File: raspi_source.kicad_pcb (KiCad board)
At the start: 2 copper layers, 18 parts, among them J1 Conn_01x02_Female, J2 Conn_01x01_Female, J3 Conn_01x01_Female, J4 Conn_01x01_Female, J5 Conn_01x02_Female, Q1 2N7000, Q2 DMG3415U, U1 OKL-T

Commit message: expand footprints
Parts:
- removed C1, C2: CP1, Capacitors_THT:CP_Radial_Tantal_D4.5mm_P2.50mm
- added CP1: 100u, Capacitors_THT:CP_Radial_Tantal_D4.5mm_P2.50mm, F.Cu at (193.0, 94.0)
- added CP2: 47u, Capacitors_THT:CP_Radial_Tantal_D4.5mm_P2.50mm, F.Cu at (160.0, 135.9)
- added CP3: 0.1u, Capacitors_THT:CP_Radial_Tantal_D4.5mm_P2.50mm, F.Cu at (130.8, 120.7)
- added Q3: 2N7000, TO_SOT_Packages_THT:TO-92_Molded_Narrow, F.Cu at (109.2, 138.4)
- added R6: 330, Resistors_THT:R_Axial_DIN0204_L3.6mm_D1.6mm_P7.62mm_Horizontal, F.Cu at (123.2, 147.3)
- added R7: 10, Resistors_THT:R_Axial_DIN0204_L3.6mm_D1.6mm_P7.62mm_Horizontal, F.Cu at (143.5, 148.6)
- R1: value R -> 470k
- R2, R3: value R -> 100k
- R4: value R -> 10k
- R5: value 1.4k -> 1k
- moved U1 82.8 mm to (213.4, 125.7)
- moved R5 68.3 mm to (212.1, 105.4)
- moved J1 53.4 mm to (142.2, 87.6)
- moved R4 49.6 mm to (208.3, 99.1)
- moved R3 47.1 mm to (184.2, 85.1)
- moved Q2 46.7 mm to (179.1, 148.6)
- moved D2 46.7 mm to (124.5, 86.4)
- moved R2 43.5 mm to (106.7, 115.6)
- moved Q1 23.9 mm to (116.8, 104.1)
- moved J5 15.3 mm to (199.4, 109.2)
- moved D1 15.2 mm to (177.8, 121.9)
- moved J3 14.5 mm to (147.3, 121.9)
- moved R1 14.4 mm to (135.9, 113.0)
- moved J2 13.5 mm to (166.4, 106.7)
- moved J4 11.4 mm to (189.2, 133.3)
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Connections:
- D3 pad 1: Net-(C1-Pad1) -> Net-(D3-Pad1)
- Q1 pad 1: GND -> Net-(Q1-Pad1)
- Q2 pad 2: Net-(Q2-Pad2) -> Net-(D3-Pad1)
- Q2 pad 3: Net-(C1-Pad1) -> Net-(CP2-Pad1)
- R1 pad 1: Net-(C1-Pad1) -> +BATT
- R4 pad 1: Net-(C2-Pad2) -> Net-(R4-Pad1)
- R5 pad 2: GND -> Net-(R5-Pad2)
- U1 pad 1: GND -> Net-(R4-Pad1)
- U1 pad 2: Net-(Q2-Pad2) -> Net-(CP2-Pad1)

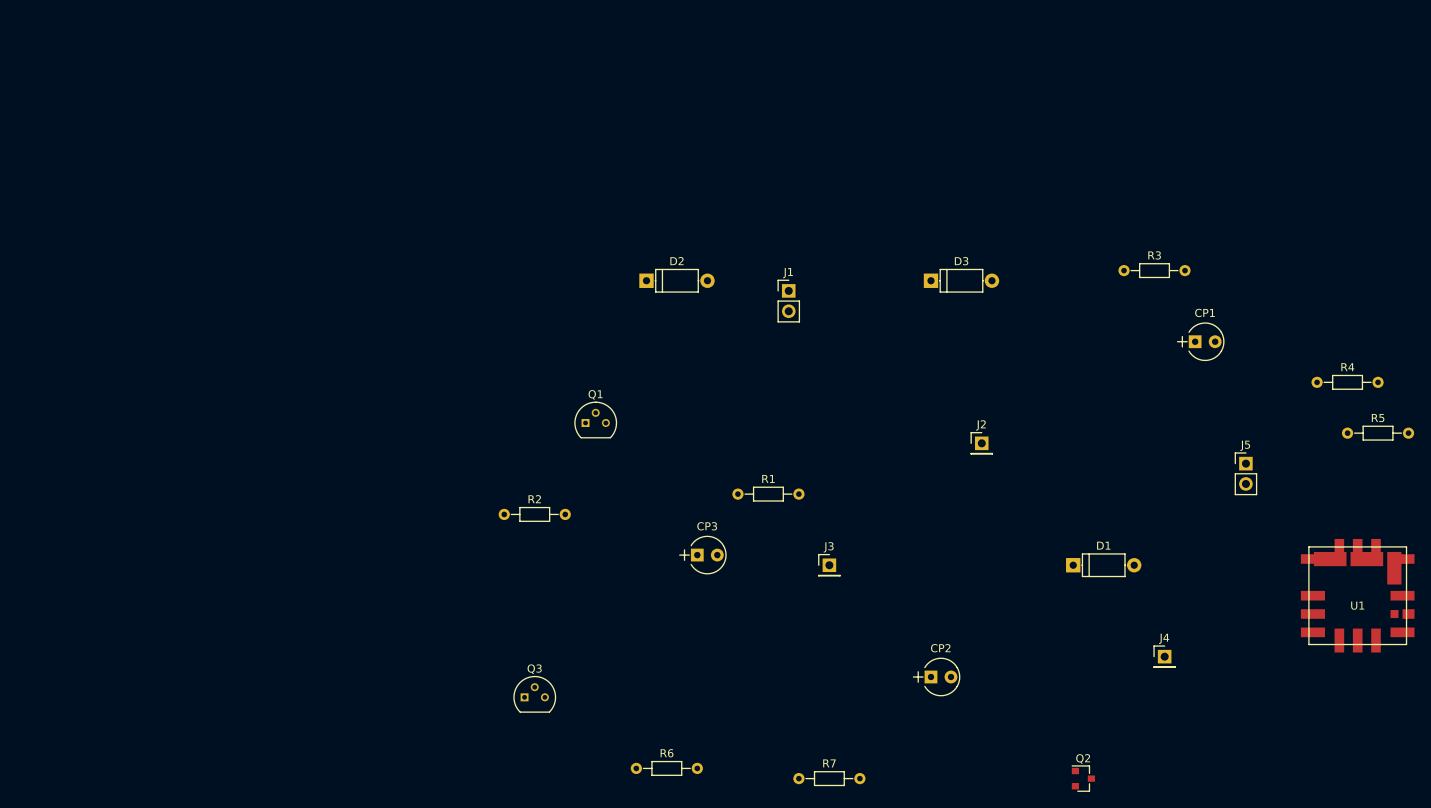
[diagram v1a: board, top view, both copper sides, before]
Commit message: wiring has been completed
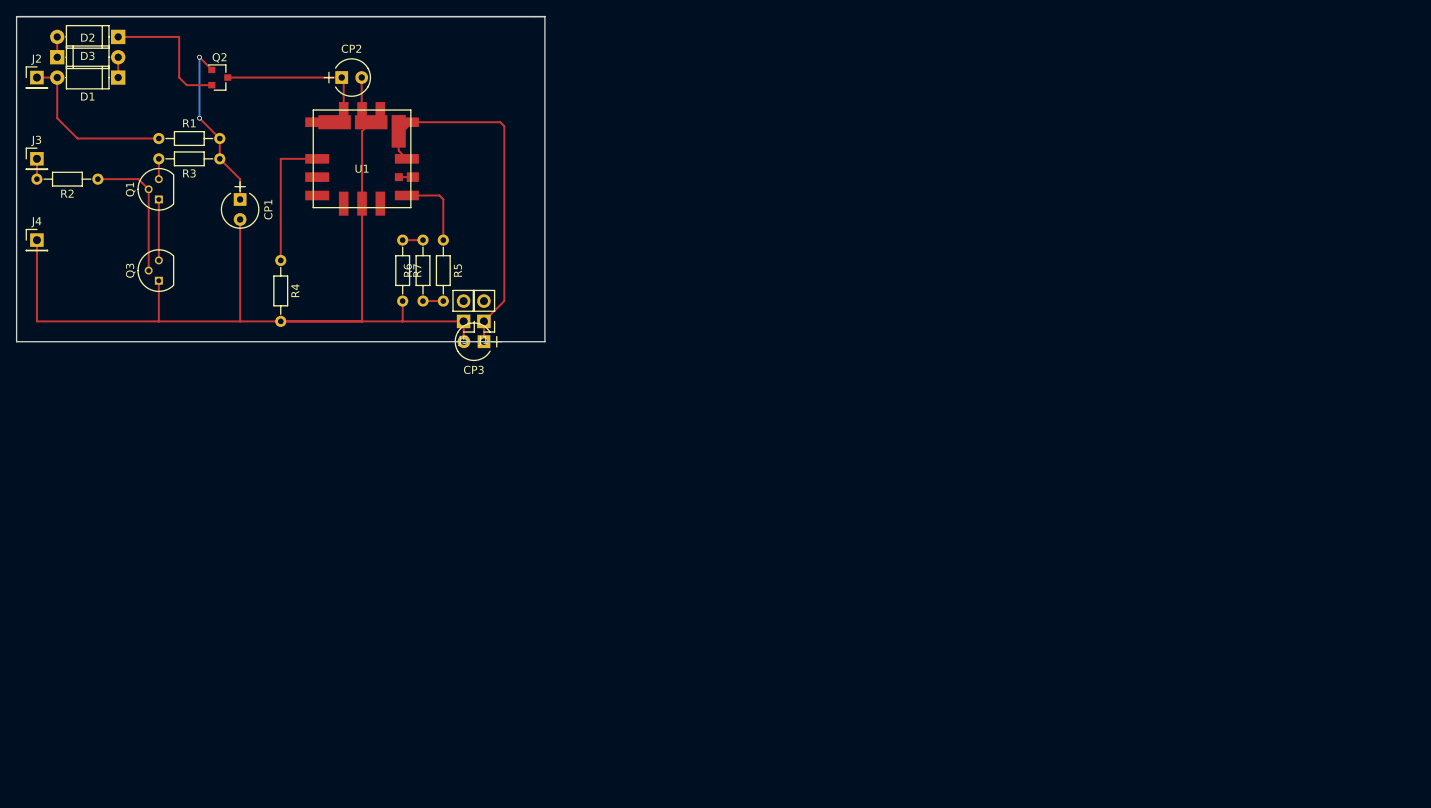
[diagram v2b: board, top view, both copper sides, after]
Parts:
- moved J4 150.3 mm to (48.3, 81.3)
- moved Q2 139.0 mm to (71.1, 61.0)
- moved U1 135.9 mm to (88.9, 71.1)
- moved D1 134.0 mm to (58.4, 61.0), turned to 180 degrees
- moved R4 130.4 mm to (78.7, 83.8), turned to 270 degrees
- moved J2 126.7 mm to (48.3, 61.0)
- moved CP1 120.7 mm to (73.7, 76.2), turned to 270 degrees
- moved R5 115.6 mm to (99.1, 81.3), turned to 270 degrees
- moved R3 113.9 mm to (71.1, 71.1), turned to 180 degrees
- moved J3 111.3 mm to (48.3, 71.1)
- moved D3 106.1 mm to (58.4, 55.9), turned to 180 degrees
- moved CP2 105.1 mm to (86.4, 61.0)
- moved J5 99.4 mm to (101.6, 91.4), turned to 180 degrees
- moved R1 84.9 mm to (63.5, 68.6)
- moved R7 83.6 mm to (94.0, 81.3), turned to 270 degrees
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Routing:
- net GND: track 0.00 -> 130.2 mm
- net Net-(CP3-Pad1): track 0.00 -> 45.7 mm
- net Net-(CP2-Pad1): track 0.00 -> 23.2 mm
- net Net-(CP1-Pad1): track 0.00 -> 22.1 mm, vias 0 -> 2
- net +BATT: track 0.00 -> 21.4 mm
- net Net-(R4-Pad1): track 0.00 -> 17.3 mm
- net Net-(D3-Pad1): track 0.00 -> 17.2 mm
- net Net-(Q1-Pad2): track 0.00 -> 17.0 mm
- net Net-(R5-Pad1): track 0.00 -> 9.85 mm
- net Net-(Q1-Pad1): track 0.00 -> 7.62 mm
- net Net-(R5-Pad2): track 0.00 -> 2.54 mm
- net Net-(D2-Pad1): track 0.00 -> 2.54 mm
- net Net-(D1-Pad1): track 0.00 -> 2.54 mm
- net Net-(R6-Pad2): track 0.00 -> 2.54 mm
- net Net-(Q1-Pad3): track 0.00 -> 2.54 mm
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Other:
- board outline added: 66 x 40.6 mm

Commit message: move capaciter
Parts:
- moved CP3 2.54 mm to (104.1, 91.4)
- moved R5 2.54 mm to (99.1, 78.7)
- moved R6 2.54 mm to (96.5, 86.4)
- moved R7 2.54 mm to (94.0, 78.7)
- moved J1 2.54 mm to (104.1, 88.9)
- moved J5 2.54 mm to (101.6, 88.9)
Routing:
- net GND: track 130.2 -> 132.8 mm
- net Net-(R5-Pad1): track 9.85 -> 7.31 mm
- net Net-(R6-Pad2): track 2.54 -> 0.00 mm
- net Net-(CP3-Pad1): track 45.7 -> 48.3 mm
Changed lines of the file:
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@@
-(kicad_pcb (version 4) (host pcbnew 4.0.7)
+(kicad_pcb (version 4) (host pcbnew 4.0.5+dfsg1-4)
   (general
     (links 37)
-    (no_connects 0)
-    (area 119.459999 89.445 193.215239 136.755)
+    (no_connects 1)
+    (area 45.644999 53.264999 111.835001 94.055001)
     (thickness 1.6)
     (drawings 6)
@@
   )
   (module Capacitors_THT:CP_Radial_Tantal_D4.5mm_P2.50mm (layer F.Cu)
-    (at 104.14 93.98 180)
+    (at 104.14 91.44 180)
     (descr "CP, Radial_Tantal series, Radial, pin pitch=2.50mm, , diameter=4.5mm, Tantal Electrolytic Capacitor, http://cdn-reichelt.de/documents/datenblatt/B300/TANTAL-TB-Serie%23.pdf")
     (tags "CP Radial_Tantal series Radial pin pitch 2.50mm  diameter 4.5mm Tantal Electrolytic Capacitor")
@@
   )
   (module Socket_Strips:Socket_Strip_Straight_1x02_Pitch2.54mm (layer F.Cu)
-    (at 104.14 91.44 180)
+    (at 104.14 88.9 180)
     (descr "Through hole straight socket strip, 1x02, 2.54mm pitch, single row")
     (tags "Through hole socket strip THT 1x02 2.54mm single row")
@@
   )
   (module Socket_Strips:Socket_Strip_Straight_1x02_Pitch2.54mm (layer F.Cu)
-    (at 101.6 91.44 180)
+    (at 101.6 88.9 180)
     (descr "Through hole straight socket strip, 1x02, 2.54mm pitch, single row")
     (tags "Through hole socket strip THT 1x02 2.54mm single row")
@@
   )
   (module Resistors_THT:R_Axial_DIN0204_L3.6mm_D1.6mm_P7.62mm_Horizontal (layer F.Cu)
-    (at 99.06 81.28 270)
+    (at 99.06 78.74 270)
     (descr "Resistor, Axial_DIN0204 series, Axial, Horizontal, pin pitch=7.62mm, 0.16666666666666666W = 1/6W, length*diameter=3.6*1.6mm^2, http://cdn-reichelt.de/documents/datenblatt/B400/1_4W%23YAG.pdf")
     (tags "Resistor Axial_DIN0204 series Axial Horizontal pin pitch 7.62mm 0.16666666666666666W = 1/6W length 3.6mm diameter 1.6mm")
@@
   )
   (module Resistors_THT:R_Axial_DIN0204_L3.6mm_D1.6mm_P7.62mm_Horizontal (layer F.Cu)
-    (at 96.52 88.9 90)
+    (at 96.52 86.36 90)
     (descr "Resistor, Axial_DIN0204 series, Axial, Horizontal, pin pitch=7.62mm, 0.16666666666666666W = 1/6W, length*diameter=3.6*1.6mm^2, http://cdn-reichelt.de/documents/datenblatt/B400/1_4W%23YAG.pdf")
     (tags "Resistor Axial_DIN0204 series Axial Horizontal pin pitch 7.62mm 0.16666666666666666W = 1/6W length 3.6mm diameter 1.6mm")
@@
   )
   (module Resistors_THT:R_Axial_DIN0204_L3.6mm_D1.6mm_P7.62mm_Horizontal (layer F.Cu)
-    (at 93.98 81.28 270)
+    (at 93.98 78.74 270)
     (descr "Resistor, Axial_DIN0204 series, Axial, Horizontal, pin pitch=7.62mm, 0.16666666666666666W = 1/6W, length*diameter=3.6*1.6mm^2, http://cdn-reichelt.de/documents/datenblatt/B400/1_4W%23YAG.pdf")
     (tags "Resistor Axial_DIN0204 series Axial Horizontal pin pitch 7.62mm 0.16666666666666666W = 1/6W length 3.6mm diameter 1.6mm")
@@
   (segment (start 73.66 78.7) (end 73.66 91.44) (width 0.25) (layer F.Cu) (net 6))
   (segment (start 63.5 86.36) (end 63.5 91.44) (width 0.25) (layer F.Cu) (net 6))
-  (segment (start 101.6 91.44) (end 101.6 93.94) (width 0.25) (layer F.Cu) (net 6))
-  (segment (start 101.6 93.94) (end 101.64 93.98) (width 0.25) (layer F.Cu) (net 6))
+  (segment (start 101.6 91.44) (end 101.6 88.9) (width 0.25) (layer F.Cu) (net 6) (status 800000))
+  (segment (start 101.6 88.9) (end 101.64 88.94) (width 0.25) (layer F.Cu) (net 6) (status 400000))
   (segment (start 88.86 60.96) (end 88.86 64.8) (width 0.25) (layer F.Cu) (net 6))
   (segment (start 88.86 64.8) (end 88.9 64.84) (width 0.25) (layer F.Cu) (net 6))
   (segment (start 78.74 91.44) (end 88.9 91.44) (width 0.25) (layer F.Cu) (net 6))
-  (segment (start 93.98 88.9) (end 93.98 91.44) (width 0.25) (layer F.Cu) (net 6))
+  (segment (start 93.98 86.36) (end 93.98 91.44) (width 0.25) (layer F.Cu) (net 6))
   (segment (start 88.9 76.72) (end 88.9 67.685) (width 0.25) (layer F.Cu) (net 6))
   (segment (start 88.9 67.685) (end 90.045 66.54) (width 0.25) (layer F.Cu) (net 6))
@@
   (segment (start 63.5 71.12) (end 63.5 73.66) (width 0.25) (layer F.Cu) (net 9))
   (segment (start 94.5 75.7) (end 98.56 75.7) (width 0.25) (layer F.Cu) (net 10))
-  (segment (start 99.06 76.2) (end 99.06 81.28) (width 0.25) (layer F.Cu) (net 10))
+  (segment (start 99.06 76.2) (end 99.06 78.74) (width 0.25) (layer F.Cu) (net 10))
   (segment (start 98.56 75.7) (end 99.06 76.2) (width 0.25) (layer F.Cu) (net 10))
-  (segment (start 93.5 73.41) (end 95.25 73.41) (width 0.25) (layer F.Cu) (net 13) (status C00000))
+  (segment (start 93.5 73.41) (end 95.25 73.41) (width 0.25) (layer F.Cu) (net 13))
   (via (at 68.58 66.04) (size 0.6) (drill 0.4) (layers F.Cu B.Cu) (net 16))
   (segment (start 71.12 68.58) (end 68.58 66.04) (width 0.25) (layer F.Cu) (net 16))
@@
   (segment (start 86.36 60.96) (end 86.61 61.21) (width 0.25) (layer F.Cu) (net 17))
   (segment (start 86.61 61.21) (end 86.61 64.84) (width 0.25) (layer F.Cu) (net 17))
-  (segment (start 104.14 93.98) (end 104.14 91.44) (width 0.25) (layer F.Cu) (net 18))
+  (segment (start 106.68 88.9) (end 104.14 88.9) (width 0.25) (layer F.Cu) (net 18) (status 800000))
+  (segment (start 104.14 88.9) (end 104.14 91.44) (width 0.25) (layer F.Cu) (net 18) (status C00000))
   (segment (start 93.485 67.685) (end 94.04 67.685) (width 0.25) (layer F.Cu) (net 18))
   (segment (start 94.04 67.685) (end 95.185 66.54) (width 0.25) (layer F.Cu) (net 18))
@@
   (segment (start 78.74 83.82) (end 78.74 71.12) (width 0.25) (layer F.Cu) (net 21))
   (segment (start 78.74 71.12) (end 83.3 71.12) (width 0.25) (layer F.Cu) (net 21))
-  (segment (start 99.06 88.9) (end 96.52 88.9) (width 0.25) (layer F.Cu) (net 22))
-  (segment (start 96.52 81.28) (end 93.98 81.28) (width 0.25) (layer F.Cu) (net 23))
+  (segment (start 96.52 86.36) (end 99.06 86.36) (width 0.25) (layer F.Cu) (net 22))
 )
